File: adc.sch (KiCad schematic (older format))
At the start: 8 parts, among them U301 ADS1261BIRHBR

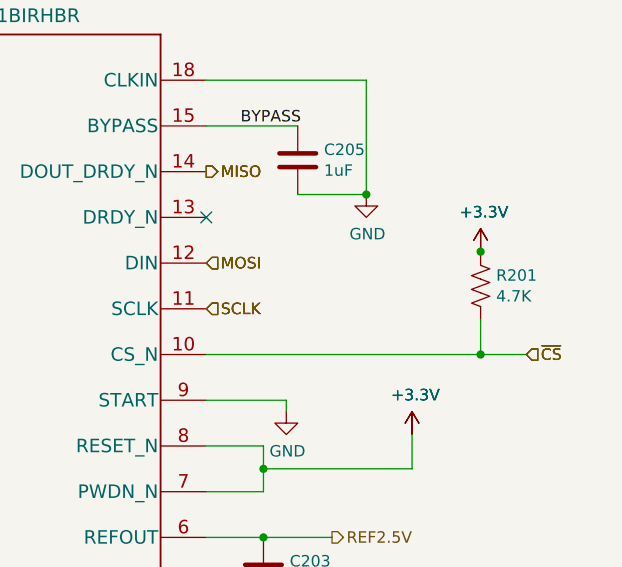
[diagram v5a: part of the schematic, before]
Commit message: placed digital gnd plane
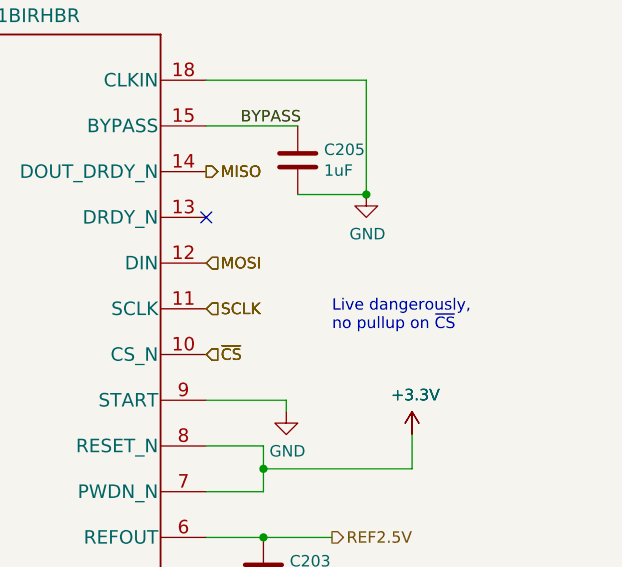
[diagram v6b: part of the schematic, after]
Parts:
- removed R201: 4.7K, Resistor_SMD:R_0805_2012Metric_Pad1.15x1.40mm_HandSolder, symbol Device:R_US
- C202, C204, C205, C301, C303, C306: footprint Capacitor_SMD:C_0805_2012Metric_Pad1.15x1.40mm_HandSolder -> Capacitor_SMD:C_0603_1608Metric_Pad1.05x0.95mm_HandSolder
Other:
- note added: "Live dangerously,\nno pullup on ~CS"
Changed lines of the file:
@@
 F 0 "C205" H 6215 1996 50  0000 L CNN
 F 1 "1uF" H 6215 1905 50  0000 L CNN
-F 2 "Capacitor_SMD:C_0805_2012Metric_Pad1.15x1.40mm_HandSolder" H 6138 1800 50  0001 C CNN
+F 2 "Capacitor_SMD:C_0603_1608Metric_Pad1.05x0.95mm_HandSolder" H 6138 1800 50  0001 C CNN
 F 3 "~" H 6100 1950 50  0001 C CNN
 	1    6100 1950
@@
 Text HLabel 5700 2600 2    50   Input ~ 0
 SCLK
-Text HLabel 7100 2800 2    50   Input ~ 0
+Text HLabel 5700 2800 2    50   Input ~ 0
 ~CS
 Text HLabel 5700 2000 2    50   Output ~ 0
@@
 F 0 "C201" H 3715 5596 50  0000 L CNN
 F 1 "4.7nF C0G" H 3715 5505 50  0000 L CNN
-F 2 "Capacitor_SMD:C_0805_2012Metric_Pad1.15x1.40mm_HandSolder" H 3638 5400 50  0001 C CNN
+F 2 "Capacitor_SMD:C_0603_1608Metric_Pad1.05x0.95mm_HandSolder" H 3638 5400 50  0001 C CNN
 F 3 "~" H 3600 5550 50  0001 C CNN
 	1    3600 5550
@@
 Text HLabel 5700 2600 2    50   Input ~ 0
 SCLK
-Text HLabel 7100 2800 2    50   Input ~ 0
+Text HLabel 5700 2800 2    50   Input ~ 0
 ~CS
 Text HLabel 5700 2000 2    50   Output ~ 0
@@
 F 0 "C202" H 3465 6096 50  0000 L CNN
 F 1 "1uF" H 3465 6005 50  0000 L CNN
-F 2 "Capacitor_SMD:C_0805_2012Metric_Pad1.15x1.40mm_HandSolder" H 3388 5900 50  0001 C CNN
+F 2 "Capacitor_SMD:C_0603_1608Metric_Pad1.05x0.95mm_HandSolder" H 3388 5900 50  0001 C CNN
 F 3 "~" H 3350 6050 50  0001 C CNN
 	1    3350 6050
@@
 F 0 "C204" H 6165 5846 50  0000 L CNN
 F 1 "1uF" H 6165 5755 50  0000 L CNN
-F 2 "Capacitor_SMD:C_0805_2012Metric_Pad1.15x1.40mm_HandSolder" H 6088 5650 50  0001 C CNN
+F 2 "Capacitor_SMD:C_0603_1608Metric_Pad1.05x0.95mm_HandSolder" H 6088 5650 50  0001 C CNN
 F 3 "~" H 6050 5800 50  0001 C CNN
 	1    6050 5800
@@
 F 0 "C206" H 3815 6096 50  0000 L CNN
 F 1 "10uF" H 3815 6005 50  0000 L CNN
-F 2 "Capacitor_SMD:C_0805_2012Metric_Pad1.15x1.40mm_HandSolder" H 3738 5900 50  0001 C CNN
+F 2 "Capacitor_SMD:C_0603_1608Metric_Pad1.05x0.95mm_HandSolder" H 3738 5900 50  0001 C CNN
 F 3 "~" H 3700 6050 50  0001 C CNN
 	1    3700 6050
@@
 F 0 "C203" H 6065 3796 50  0000 L CNN
 F 1 "10uF" H 6065 3705 50  0000 L CNN
-F 2 "Capacitor_SMD:C_0805_2012Metric_Pad1.15x1.40mm_HandSolder" H 5988 3600 50  0001 C CNN
+F 2 "Capacitor_SMD:C_0603_1608Metric_Pad1.05x0.95mm_HandSolder" H 5988 3600 50  0001 C CNN
 F 3 "~" H 5950 3750 50  0001 C CNN
 	1    5950 3750
@@
 	5950 3400 5950 3300
 Connection ~ 5950 3300
-$Comp
-L Device:R_US R201
-U 1 1 5F6B4ED7
-P 6900 2500
-AR Path="/5F4A8EC5/5F6B4ED7" Ref="R201"  Part="1"
-AR Path="/5F4D3EB7/5F6B4ED7" Ref="R301"  Part="1"
-F 0 "R201" H 6968 2546 50  0000 L CNN
-F 1 "4.7K" H 6968 2455 50  0000 L CNN
-F 2 "Resistor_SMD:R_0805_2012Metric_Pad1.15x1.40mm_HandSolder" V 6940 2490 50  0001 C CNN
-F 3 "~" H 6900 2500 50  0001 C CNN
-	1    6900 2500
-	1    0    0    -1
-$EndComp
-$Comp
-L power:+3.3V #PWR0104
-U 1 1 5F6B97FB
-P 6900 2350
-AR Path="/5F4A8EC5/5F6B97FB" Ref="#PWR0104"  Part="1"
-AR Path="/5F4D3EB7/5F6B97FB" Ref="#PWR0128"  Part="1"
-F 0 "#PWR0104" H 6900 2200 50  0001 C CNN
-F 1 "+3.3V" H 6915 2523 50  0000 C CNN
-F 2 "" H 6900 2350 50  0001 C CNN
-F 3 "" H 6900 2350 50  0001 C CNN
-	1    6900 2350
-	1    0    0    -1
-$EndComp
-$Comp
-L power:+3.3V #PWR0130
-U 1 1 5F6B9801
-P 6900 2350
-AR Path="/5F4D3EB7/5F6B9801" Ref="#PWR0130"  Part="1"
-AR Path="/5F4A8EC5/5F6B9801" Ref="#PWR0105"  Part="1"
-F 0 "#PWR0105" H 6900 2200 50  0001 C CNN
-F 1 "+3.3V" H 6915 2523 50  0000 C CNN
-F 2 "" H 6900 2350 50  0001 C CNN
-F 3 "" H 6900 2350 50  0001 C CNN
-	1    6900 2350
-	1    0    0    -1
-$EndComp
-Connection ~ 6900 2350
-Wire Wire Line
-	5700 2800 6900 2800
-Wire Wire Line
-	6900 2650 6900 2800
-Connection ~ 6900 2800
-Wire Wire Line
-	6900 2800 7100 2800
 NoConn ~ 3900 1600
 NoConn ~ 3900 1700
@@
 Text Label 3450 5900 0    50   ~ 0
 APWR
+Text Notes 6250 2700 0    50   ~ 0
+Live dangerously,\nno pullup on ~CS
 $EndSCHEMATC

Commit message: temporarily complete
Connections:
- net +3V3 is gone; now on net +5V: C204.1, U301.17 (DVDD), U301.7 (PWDN_N), U301.8 (RESET_N)
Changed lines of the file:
@@
 $Descr A4 11693 8268
 encoding utf-8
-Sheet 2 4
+Sheet 3 4
 Title ""
 Date ""
@@
 Wire Wire Line
 	3200 5900 3200 5750
-$Comp
-L power:+5V #PWR0107
-U 1 1 5F4D602B
-P 3200 5750
-AR Path="/5F4A8EC5/5F4D602B" Ref="#PWR0107"  Part="1"
-AR Path="/5F4D3EB7/5F4D602B" Ref="#PWR0123"  Part="1"
-F 0 "#PWR0107" H 3200 5600 50  0001 C CNN
-F 1 "+5V" H 3215 5923 50  0000 C CNN
-F 2 "" H 3200 5750 50  0001 C CNN
-F 3 "" H 3200 5750 50  0001 C CNN
-	1    3200 5750
-	1    0    0    -1
-$EndComp
 Wire Wire Line
 	3900 5700 3600 5700
@@
 AR Path="/5F4A8EC5/5F4ADFB1" Ref="#PWR0108"  Part="1"
 AR Path="/5F4D3EB7/5F4ADFB1" Ref="#PWR0124"  Part="1"
-F 0 "#PWR0108" H 3700 6050 50  0001 C CNN
+F 0 "#PWR0124" H 3700 6050 50  0001 C CNN
 F 1 "GNDREF" H 3705 6127 50  0000 C CNN
 F 2 "" H 3700 6300 50  0001 C CNN
@@
 AR Path="/5F4A8EC5/5F4AF0E5" Ref="#PWR0109"  Part="1"
 AR Path="/5F4D3EB7/5F4AF0E5" Ref="#PWR0125"  Part="1"
-F 0 "#PWR0109" H 5850 6050 50  0001 C CNN
+F 0 "#PWR0125" H 5850 6050 50  0001 C CNN
 F 1 "GND" H 5855 6127 50  0000 C CNN
 F 2 "" H 5850 6300 50  0001 C CNN
@@
 Wire Wire Line
 	5850 6300 5700 6300
-$Comp
-L power:+3.3V #PWR0110
-U 1 1 5F4B0081
-P 6050 5650
-AR Path="/5F4A8EC5/5F4B0081" Ref="#PWR0110"  Part="1"
-AR Path="/5F4D3EB7/5F4B0081" Ref="#PWR0126"  Part="1"
-F 0 "#PWR0110" H 6050 5500 50  0001 C CNN
-F 1 "+3.3V" H 6065 5823 50  0000 C CNN
-F 2 "" H 6050 5650 50  0001 C CNN
-F 3 "" H 6050 5650 50  0001 C CNN
-	1    6050 5650
-	1    0    0    -1
-$EndComp
 Wire Wire Line
 	5700 3000 6050 3000
 Wire Wire Line
 	6050 3000 6050 3050
-$Comp
-L power:+3.3V #PWR0113
-U 1 1 5F4D6031
-P 6600 3150
-AR Path="/5F4A8EC5/5F4D6031" Ref="#PWR0113"  Part="1"
-AR Path="/5F4D3EB7/5F4D6031" Ref="#PWR0129"  Part="1"
-F 0 "#PWR0113" H 6600 3000 50  0001 C CNN
-F 1 "+3.3V" H 6615 3323 50  0000 C CNN
-F 2 "" H 6600 3150 50  0001 C CNN
-F 3 "" H 6600 3150 50  0001 C CNN
-	1    6600 3150
-	1    0    0    -1
-$EndComp
 NoConn ~ 5700 2200
 $Comp
@@
 AR Path="/5F4A8EC5/5F4B6004" Ref="C205"  Part="1"
 AR Path="/5F4D3EB7/5F4B6004" Ref="C305"  Part="1"
-F 0 "C205" H 6215 1996 50  0000 L CNN
+F 0 "C305" H 6215 1996 50  0000 L CNN
 F 1 "1uF" H 6215 1905 50  0000 L CNN
 F 2 "Capacitor_SMD:C_0603_1608Metric_Pad1.05x0.95mm_HandSolder" H 6138 1800 50  0001 C CNN
@@
 AR Path="/5F4D3EB7/5F4A90E1" Ref="U301"  Part="1"
 AR Path="/5F4A8EC5/5F4A90E1" Ref="U201"  Part="1"
-F 0 "U201" H 4800 6588 60  0000 C CNN
+F 0 "U301" H 4800 6588 60  0000 C CNN
 F 1 "ADS1261BIRHBR" H 4800 6482 60  0000 C CNN
 F 2 "Package_DFN_QFN:Texas_S-PVQFN-N32_EP3.45x3.45mm" H 4800 3840 60  0001 C CNN
@@
 AR Path="/5F4D3EB7/5F4AAB9D" Ref="C301"  Part="1"
 AR Path="/5F4A8EC5/5F4AAB9D" Ref="C201"  Part="1"
-F 0 "C201" H 3715 5596 50  0000 L CNN
+F 0 "C301" H 3715 5596 50  0000 L CNN
 F 1 "4.7nF C0G" H 3715 5505 50  0000 L CNN
 F 2 "Capacitor_SMD:C_0603_1608Metric_Pad1.05x0.95mm_HandSolder" H 3638 5400 50  0001 C CNN
@@
 AR Path="/5F4D3EB7/5F4ABE0F" Ref="#PWR0131"  Part="1"
 AR Path="/5F4A8EC5/5F4ABE0F" Ref="#PWR0115"  Part="1"
-F 0 "#PWR0115" H 3200 5600 50  0001 C CNN
+F 0 "#PWR0131" H 3200 5600 50  0001 C CNN
 F 1 "+5V" H 3215 5923 50  0000 C CNN
 F 2 "" H 3200 5750 50  0001 C CNN
@@
 AR Path="/5F4D3EB7/5F4D602C" Ref="#PWR0132"  Part="1"
 AR Path="/5F4A8EC5/5F4D602C" Ref="#PWR0116"  Part="1"
-F 0 "#PWR0116" H 3700 6050 50  0001 C CNN
+F 0 "#PWR0132" H 3700 6050 50  0001 C CNN
 F 1 "GNDREF" H 3705 6127 50  0000 C CNN
 F 2 "" H 3700 6300 50  0001 C CNN
@@
 AR Path="/5F4D3EB7/5F4D602D" Ref="#PWR0133"  Part="1"
 AR Path="/5F4A8EC5/5F4D602D" Ref="#PWR0117"  Part="1"
-F 0 "#PWR0117" H 5850 6050 50  0001 C CNN
+F 0 "#PWR0133" H 5850 6050 50  0001 C CNN
 F 1 "GND" H 5855 6127 50  0000 C CNN
 F 2 "" H 5850 6300 50  0001 C CNN
 F 3 "" H 5850 6300 50  0001 C CNN
 	1    5850 6300
-	1    0    0    -1
-$EndComp
-$Comp
-L power:+3.3V #PWR0134
-U 1 1 5F4D602E
-P 6050 5650
-AR Path="/5F4D3EB7/5F4D602E" Ref="#PWR0134"  Part="1"
-AR Path="/5F4A8EC5/5F4D602E" Ref="#PWR0118"  Part="1"
-F 0 "#PWR0118" H 6050 5500 50  0001 C CNN
-F 1 "+3.3V" H 6065 5823 50  0000 C CNN
-F 2 "" H 6050 5650 50  0001 C CNN
-F 3 "" H 6050 5650 50  0001 C CNN
-	1    6050 5650
 	1    0    0    -1
 $EndComp
@@
 AR Path="/5F4D3EB7/5F4D6030" Ref="#PWR0136"  Part="1"
 AR Path="/5F4A8EC5/5F4D6030" Ref="#PWR0120"  Part="1"
-F 0 "#PWR0120" H 6050 2800 50  0001 C CNN
+F 0 "#PWR0136" H 6050 2800 50  0001 C CNN
 F 1 "GND" H 6055 2877 50  0000 C CNN
 F 2 "" H 6050 3050 50  0001 C CNN
 F 3 "" H 6050 3050 50  0001 C CNN
 	1    6050 3050
-	1    0    0    -1
-$EndComp
-$Comp
-L power:+3.3V #PWR0137
-U 1 1 5F4B3879
-P 6600 3150
-AR Path="/5F4D3EB7/5F4B3879" Ref="#PWR0137"  Part="1"
-AR Path="/5F4A8EC5/5F4B3879" Ref="#PWR0121"  Part="1"
-F 0 "#PWR0121" H 6600 3000 50  0001 C CNN
-F 1 "+3.3V" H 6615 3323 50  0000 C CNN
-F 2 "" H 6600 3150 50  0001 C CNN
-F 3 "" H 6600 3150 50  0001 C CNN
-	1    6600 3150
 	1    0    0    -1
 $EndComp
@@
 Text HLabel 6250 3600 2    50   Output ~ 0
 REF2.5V
-Connection ~ 3200 5750
 Connection ~ 3700 6300
-Connection ~ 6050 5650
 Connection ~ 5850 6300
 Text Label 3650 5400 0    50   ~ 0
@@
 AR Path="/5F4A8EC5/5F4B7BDA" Ref="C202"  Part="1"
 AR Path="/5F4D3EB7/5F4B7BDA" Ref="C302"  Part="1"
-F 0 "C202" H 3465 6096 50  0000 L CNN
+F 0 "C302" H 3465 6096 50  0000 L CNN
 F 1 "1uF" H 3465 6005 50  0000 L CNN
 F 2 "Capacitor_SMD:C_0603_1608Metric_Pad1.05x0.95mm_HandSolder" H 3388 5900 50  0001 C CNN
@@
 AR Path="/5F4A8EC5/5F4CD7CF" Ref="C204"  Part="1"
 AR Path="/5F4D3EB7/5F4CD7CF" Ref="C304"  Part="1"
-F 0 "C204" H 6165 5846 50  0000 L CNN
+F 0 "C304" H 6165 5846 50  0000 L CNN
 F 1 "1uF" H 6165 5755 50  0000 L CNN
 F 2 "Capacitor_SMD:C_0603_1608Metric_Pad1.05x0.95mm_HandSolder" H 6088 5650 50  0001 C CNN
@@
 AR Path="/5F4D3EB7/5F4D602F" Ref="#PWR0135"  Part="1"
 AR Path="/5F4A8EC5/5F4D602F" Ref="#PWR0119"  Part="1"
-F 0 "#PWR0119" H 6400 1850 50  0001 C CNN
+F 0 "#PWR0135" H 6400 1850 50  0001 C CNN
 F 1 "GND" H 6405 1927 50  0000 C CNN
 F 2 "" H 6400 2100 50  0001 C CNN
@@
 AR Path="/5F4A8EC5/5F4C03A0" Ref="#PWR0111"  Part="1"
 AR Path="/5F4D3EB7/5F4C03A0" Ref="#PWR0112"  Part="1"
-F 0 "#PWR0111" H 5950 3650 50  0001 C CNN
+F 0 "#PWR0112" H 5950 3650 50  0001 C CNN
 F 1 "GNDREF" H 5955 3727 50  0000 C CNN
 F 2 "" H 5950 3900 50  0001 C CNN
@@
 AR Path="/5F4D3EB7/5F4C2005" Ref="C306"  Part="1"
 AR Path="/5F4A8EC5/5F4C2005" Ref="C206"  Part="1"
-F 0 "C206" H 3815 6096 50  0000 L CNN
+F 0 "C306" H 3815 6096 50  0000 L CNN
 F 1 "10uF" H 3815 6005 50  0000 L CNN
 F 2 "Capacitor_SMD:C_0603_1608Metric_Pad1.05x0.95mm_HandSolder" H 3738 5900 50  0001 C CNN
@@
 AR Path="/5F4D3EB7/5F4B8109" Ref="C303"  Part="1"
 AR Path="/5F4A8EC5/5F4B8109" Ref="C203"  Part="1"
-F 0 "C203" H 6065 3796 50  0000 L CNN
+F 0 "C303" H 6065 3796 50  0000 L CNN
 F 1 "10uF" H 6065 3705 50  0000 L CNN
 F 2 "Capacitor_SMD:C_0603_1608Metric_Pad1.05x0.95mm_HandSolder" H 5988 3600 50  0001 C CNN
@@
 NoConn ~ 3900 1800
 NoConn ~ 3900 1900
-Text Label 5750 5650 0    50   ~ 0
+Text Label 5800 5650 0    50   ~ 0
 DPWR
 Text Label 3450 5900 0    50   ~ 0
@@
 Text Notes 6250 2700 0    50   ~ 0
 Live dangerously,\nno pullup on ~CS
+$Comp
+L power:+5V #PWR0107
+U 1 1 5F81618F
+P 6600 3150
+AR Path="/5F4D3EB7/5F81618F" Ref="#PWR0107"  Part="1"
+AR Path="/5F4A8EC5/5F81618F" Ref="#PWR0104"  Part="1"
+F 0 "#PWR0107" H 6600 3000 50  0001 C CNN
+F 1 "+5V" H 6615 3323 50  0000 C CNN
+F 2 "" H 6600 3150 50  0001 C CNN
+F 3 "" H 6600 3150 50  0001 C CNN
+	1    6600 3150
+	1    0    0    -1
+$EndComp
+$Comp
+L power:+5V #PWR0110
+U 1 1 5F817385
+P 6050 5650
+AR Path="/5F4D3EB7/5F817385" Ref="#PWR0110"  Part="1"
+AR Path="/5F4A8EC5/5F817385" Ref="#PWR0105"  Part="1"
+F 0 "#PWR0110" H 6050 5500 50  0001 C CNN
+F 1 "+5V" H 6065 5823 50  0000 C CNN
+F 2 "" H 6050 5650 50  0001 C CNN
+F 3 "" H 6050 5650 50  0001 C CNN
+	1    6050 5650
+	1    0    0    -1
+$EndComp
+Connection ~ 6050 5650
 $EndSCHEMATC

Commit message: without silkscreen
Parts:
- C202, C204, C205, C301, C303, C306: footprint Capacitor_SMD:C_0603_1608Metric_Pad1.05x0.95mm_HandSolder -> Capacitor_SMD:C_0805_2012Metric_Pad1.15x1.40mm_HandSolder
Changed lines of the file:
@@
 F 0 "C305" H 6215 1996 50  0000 L CNN
 F 1 "1uF" H 6215 1905 50  0000 L CNN
-F 2 "Capacitor_SMD:C_0603_1608Metric_Pad1.05x0.95mm_HandSolder" H 6138 1800 50  0001 C CNN
+F 2 "Capacitor_SMD:C_0805_2012Metric_Pad1.15x1.40mm_HandSolder" H 6138 1800 50  0001 C CNN
 F 3 "~" H 6100 1950 50  0001 C CNN
 	1    6100 1950
@@
 F 0 "C301" H 3715 5596 50  0000 L CNN
 F 1 "4.7nF C0G" H 3715 5505 50  0000 L CNN
-F 2 "Capacitor_SMD:C_0603_1608Metric_Pad1.05x0.95mm_HandSolder" H 3638 5400 50  0001 C CNN
+F 2 "Capacitor_SMD:C_0805_2012Metric_Pad1.15x1.40mm_HandSolder" H 3638 5400 50  0001 C CNN
 F 3 "~" H 3600 5550 50  0001 C CNN
 	1    3600 5550
@@
 F 0 "C302" H 3465 6096 50  0000 L CNN
 F 1 "1uF" H 3465 6005 50  0000 L CNN
-F 2 "Capacitor_SMD:C_0603_1608Metric_Pad1.05x0.95mm_HandSolder" H 3388 5900 50  0001 C CNN
+F 2 "Capacitor_SMD:C_0805_2012Metric_Pad1.15x1.40mm_HandSolder" H 3388 5900 50  0001 C CNN
 F 3 "~" H 3350 6050 50  0001 C CNN
 	1    3350 6050
@@
 F 0 "C304" H 6165 5846 50  0000 L CNN
 F 1 "1uF" H 6165 5755 50  0000 L CNN
-F 2 "Capacitor_SMD:C_0603_1608Metric_Pad1.05x0.95mm_HandSolder" H 6088 5650 50  0001 C CNN
+F 2 "Capacitor_SMD:C_0805_2012Metric_Pad1.15x1.40mm_HandSolder" H 6088 5650 50  0001 C CNN
 F 3 "~" H 6050 5800 50  0001 C CNN
 	1    6050 5800
@@
 F 0 "C306" H 3815 6096 50  0000 L CNN
 F 1 "10uF" H 3815 6005 50  0000 L CNN
-F 2 "Capacitor_SMD:C_0603_1608Metric_Pad1.05x0.95mm_HandSolder" H 3738 5900 50  0001 C CNN
+F 2 "Capacitor_SMD:C_0805_2012Metric_Pad1.15x1.40mm_HandSolder" H 3738 5900 50  0001 C CNN
 F 3 "~" H 3700 6050 50  0001 C CNN
 	1    3700 6050
@@
 F 0 "C303" H 6065 3796 50  0000 L CNN
 F 1 "10uF" H 6065 3705 50  0000 L CNN
-F 2 "Capacitor_SMD:C_0603_1608Metric_Pad1.05x0.95mm_HandSolder" H 5988 3600 50  0001 C CNN
+F 2 "Capacitor_SMD:C_0805_2012Metric_Pad1.15x1.40mm_HandSolder" H 5988 3600 50  0001 C CNN
 F 3 "~" H 5950 3750 50  0001 C CNN
 	1    5950 3750
